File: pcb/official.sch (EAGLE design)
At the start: 25 parts, among them P1 DEV_CLP-150, P11 DEV_1X40

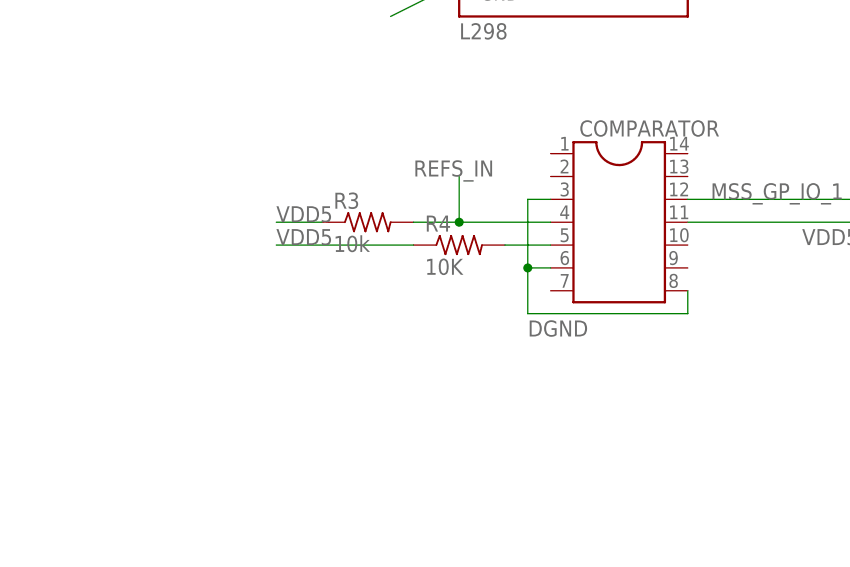
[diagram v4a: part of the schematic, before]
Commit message: Added right resistors for comparator
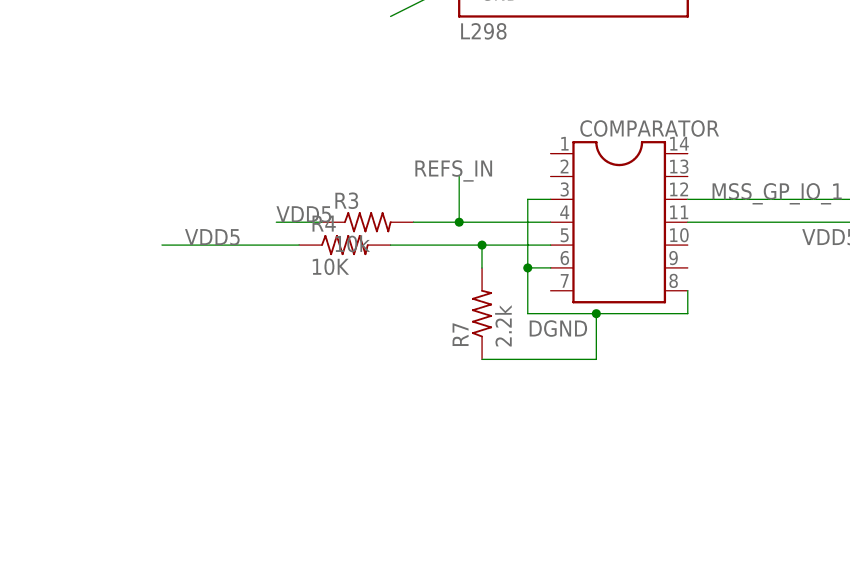
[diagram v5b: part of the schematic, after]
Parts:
- added R7: 2.2k, rcl:R-US_0309/12
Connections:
- net DGND: now also R7.1
- net N$3: now also R7.2
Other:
- moved on the sheet: R4

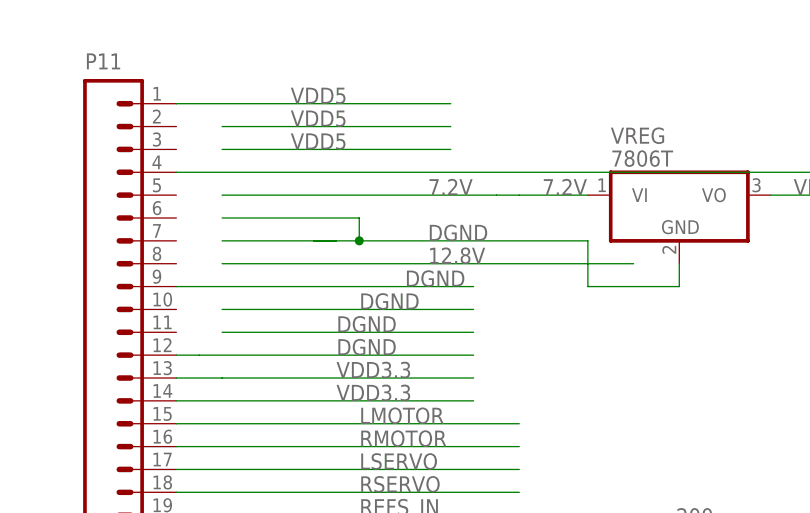
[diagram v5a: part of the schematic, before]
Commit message: Updated pins and attempt to put layers in eagle
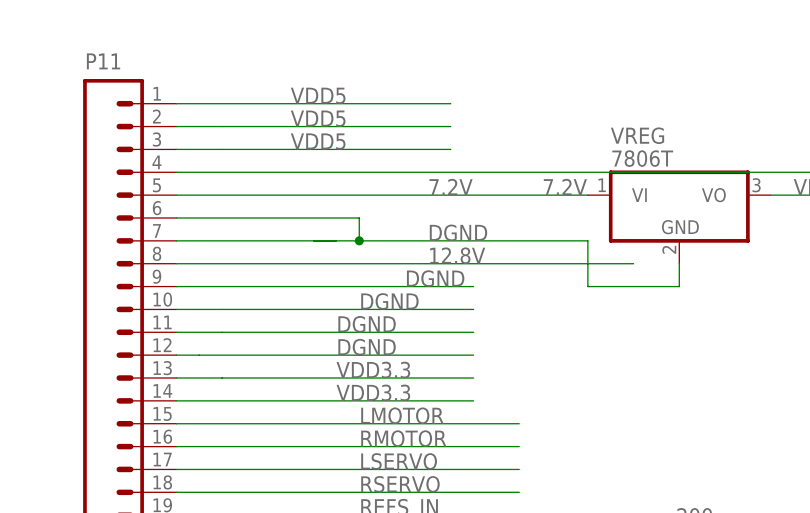
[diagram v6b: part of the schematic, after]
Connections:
- net 12.8V: now also P11.8
- net 7.2V: now also P11.5
- net DGND: now also P11.10, P11.11, P11.6, P11.7
- net VDD5: now also P11.2, P11.3
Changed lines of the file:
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@@
 </segment>
 <segment>
-<wire x1="55.88" y1="66.04" x2="71.12" y2="66.04" width="0.1524" layer="91"/>
+<wire x1="50.8" y1="66.04" x2="71.12" y2="66.04" width="0.1524" layer="91"/>
 <label x="78.74" y="66.04" size="1.778" layer="95"/>
 <wire x1="71.12" y1="66.04" x2="96.52" y2="66.04" width="0.1524" layer="91"/>
-<wire x1="55.88" y1="68.58" x2="71.12" y2="68.58" width="0.1524" layer="91"/>
+<wire x1="50.8" y1="68.58" x2="71.12" y2="68.58" width="0.1524" layer="91"/>
 <wire x1="71.12" y1="68.58" x2="71.12" y2="66.04" width="0.1524" layer="91"/>
 <junction x="71.12" y="66.04"/>
@@
 <wire x1="106.68" y1="60.96" x2="96.52" y2="60.96" width="0.1524" layer="91"/>
 <wire x1="96.52" y1="60.96" x2="96.52" y2="66.04" width="0.1524" layer="91"/>
+<pinref part="P11" gate="G$1" pin="7"/>
+<pinref part="P11" gate="G$1" pin="6"/>
 </segment>
 <segment>
@@
 <wire x1="55.88" y1="58.42" x2="83.82" y2="58.42" width="0.2032" layer="91"/>
 <label x="71.12" y="58.42" size="1.778" layer="95"/>
+<pinref part="P11" gate="G$1" pin="10"/>
+<wire x1="55.88" y1="58.42" x2="50.8" y2="58.42" width="0.1524" layer="91"/>
 </segment>
 <segment>
 <wire x1="55.88" y1="55.88" x2="83.82" y2="55.88" width="0.2032" layer="91"/>
 <label x="68.58" y="55.88" size="1.778" layer="95"/>
+<pinref part="P11" gate="G$1" pin="11"/>
+<wire x1="55.88" y1="55.88" x2="50.8" y2="55.88" width="0.1524" layer="91"/>
 </segment>
 <segment>
@@
 <label x="63.5" y="78.74" size="1.778" layer="95"/>
 <label x="63.5" y="76.2" size="1.778" layer="95"/>
+<pinref part="P11" gate="G$1" pin="3"/>
+<wire x1="55.88" y1="76.2" x2="50.8" y2="76.2" width="0.1524" layer="91"/>
+<pinref part="P11" gate="G$1" pin="2"/>
+<wire x1="55.88" y1="78.74" x2="50.8" y2="78.74" width="0.1524" layer="91"/>
 </segment>
 <segment>
@@
 <segment>
 <pinref part="VREG" gate="A1" pin="VI"/>
-<wire x1="96.52" y1="71.12" x2="88.9" y2="71.12" width="0.1524" layer="91"/>
 <label x="91.44" y="71.12" size="1.778" layer="95"/>
-<wire x1="55.88" y1="71.12" x2="86.36" y2="71.12" width="0.1524" layer="91"/>
+<wire x1="50.8" y1="71.12" x2="96.52" y2="71.12" width="0.1524" layer="91"/>
 <label x="78.74" y="71.12" size="1.778" layer="95"/>
-<wire x1="86.36" y1="71.12" x2="88.9" y2="71.12" width="0.1524" layer="91"/>
+<pinref part="P11" gate="G$1" pin="5"/>
 </segment>
 </net>
@@
 </segment>
 <segment>
-<wire x1="55.88" y1="63.5" x2="101.6" y2="63.5" width="0.1524" layer="91"/>
+<wire x1="50.8" y1="63.5" x2="101.6" y2="63.5" width="0.1524" layer="91"/>
 <label x="78.74" y="63.5" size="1.778" layer="95"/>
-</segment>
-</net>
+<pinref part="P11" gate="G$1" pin="8"/>
+</segment>
+</net>
